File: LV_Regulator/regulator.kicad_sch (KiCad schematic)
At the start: 23 parts, among them U5 BQ25858QWRRVRQ1, U6 CSD19506KTT, U7 CSD19506KTT, U8 CSD19506KTT, U9 CSD19506KTT

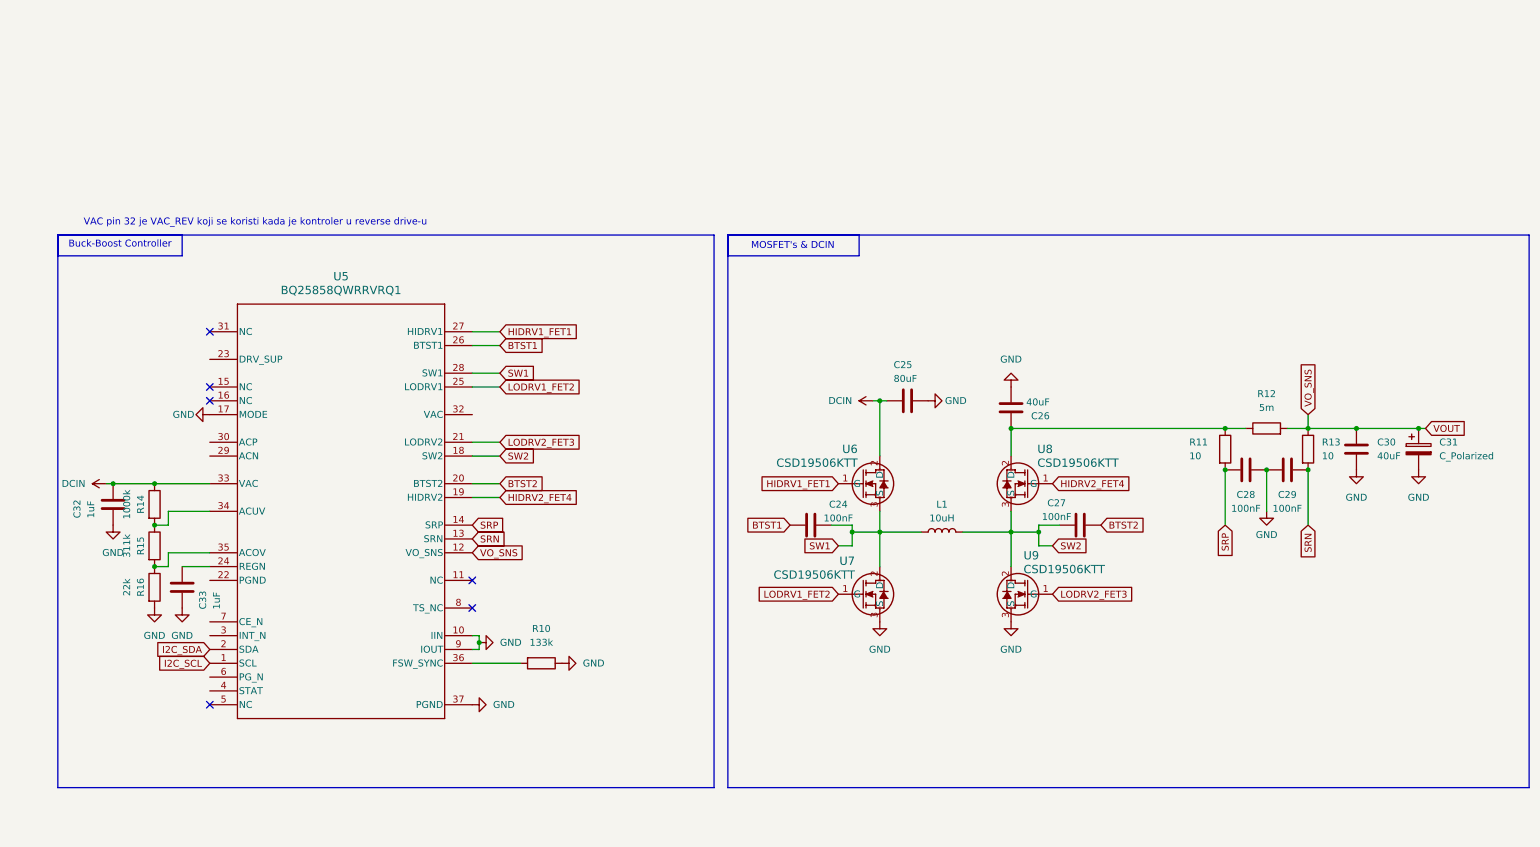
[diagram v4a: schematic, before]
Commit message: Update & Further Progress on Regulator Controller Schematic
Nikola Popovic added Frequency choice jumpers
I added Jumpers for Voltage trigger selection
Made global Labels for MCU pin connection, connected PG & STAT Diodes as well as connected ACN & ACP pins.
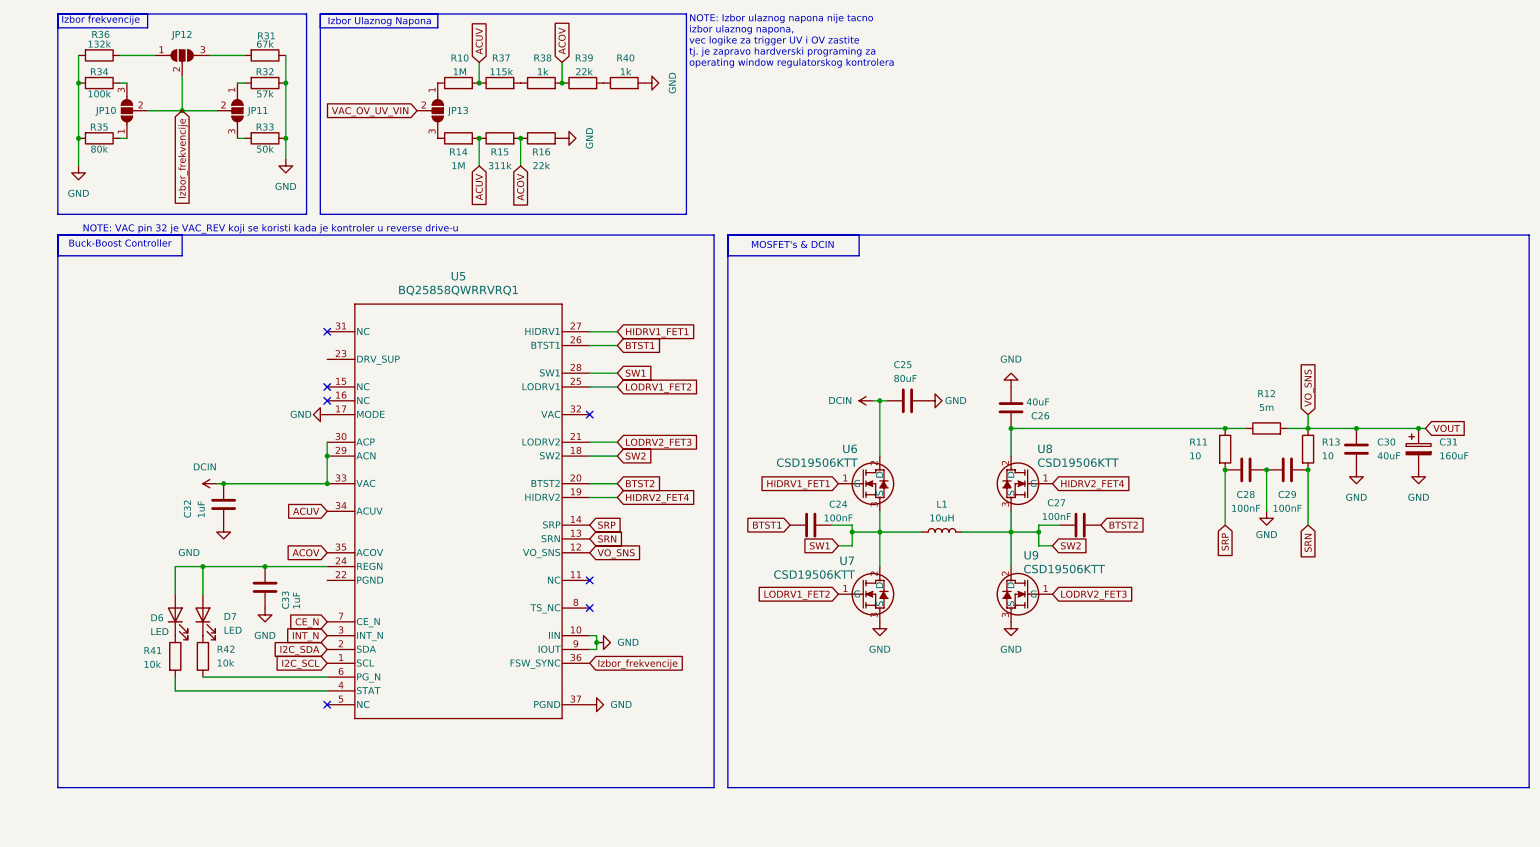
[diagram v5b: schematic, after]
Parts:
- added D6, D7: LED, symbol Device:LED
- added JP10, JP11, JP12, JP13: SolderJumper_3_Open, symbol Jumper:SolderJumper_3_Open
- added R31: 67k, symbol Device:R
- added R32: 57k, symbol Device:R
- added R33: 50k, symbol Device:R
- added R34: 100k, symbol Device:R
- added R35: 80k, symbol Device:R
- added R36: 132k, symbol Device:R
- added R37: 115k, symbol Device:R
- added R38, R40: 1k, symbol Device:R
- added R39: 22k, symbol Device:R
- added R41, R42: 10k, symbol Device:R
- C31: value C_Polarized -> 160uF
- R10: value 133k -> 1M
- R14: value 1000k -> 1M
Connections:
- net DCIN: now also U5.29 (ACN), U5.30 (ACP); no longer R14.1
- net GND: now also R31.1, R32.1, R33.1, R34.2, R35.2, R36.2, R40.2; no longer R10.1
- net ACOV: now reaches R15.2, R16.1, U5.35 (ACOV)
- net ACOV: now also R38.2, R39.1
- net ACUV: now reaches R10.2
- net ACUV: now also R14.2, R15.1, U5.34 (ACUV), R37.1; no longer U5.36 (FSW_SYNC)
- net at C33.2, U5.24 (REGN): now also D6.2 (A), D7.2 (A)
- net INT_N: now reaches U5.3 (INT_N)
- net at U5.4 (STAT): now also R41.2
- net at U5.6 (PG_N): now also R42.2
- net CE_N: now reaches U5.7 (CE_N)
- new net: D6.1 (K), R41.1
- new net: R37.2, R38.1
- new net: JP10.1 (A), R35.1
- new net: D7.1 (K), R42.1
- new net: R39.2, R40.1
- new net: JP12.3 (B), R31.2
- new net: JP10.3 (B), R34.1
- new net: JP11.3 (B), R33.2
- new net: JP11.1 (A), R32.2
- new net: JP13.3 (B), R14.1
- new net: JP13.1 (A), R10.1
- new net: JP12.1 (A), R36.1
- new net Izbor_frekvencije: JP10.2 (C), JP11.2 (C), JP12.2 (C), U5.36 (FSW_SYNC)
- new net VAC_OV_UV_VIN: JP13.2 (C)
- no-connect marks 6 -> 7
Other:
- note added: "Izbor Ulaznog Napona"
- note added: "Izbor frekvencije"
- note added: "NOTE: Izbor ulaznog napona nije tacno izbor ulaznog napona, vec logike za trigger UV i OV zastite tj. je zapravo hardverski programing za operating window regulatorskog kontrolera"
- note added: "NOTE: VAC pin 32 je VAC_REV koji se koristi kada je kontroler u reverse drive-u"
- note removed: "VAC pin 32 je VAC_REV koji se koristi kada je kontroler u reverse drive-u"
- moved on the sheet: C32, C33, R14, R15, R16, U5
